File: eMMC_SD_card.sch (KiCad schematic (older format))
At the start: 0 parts

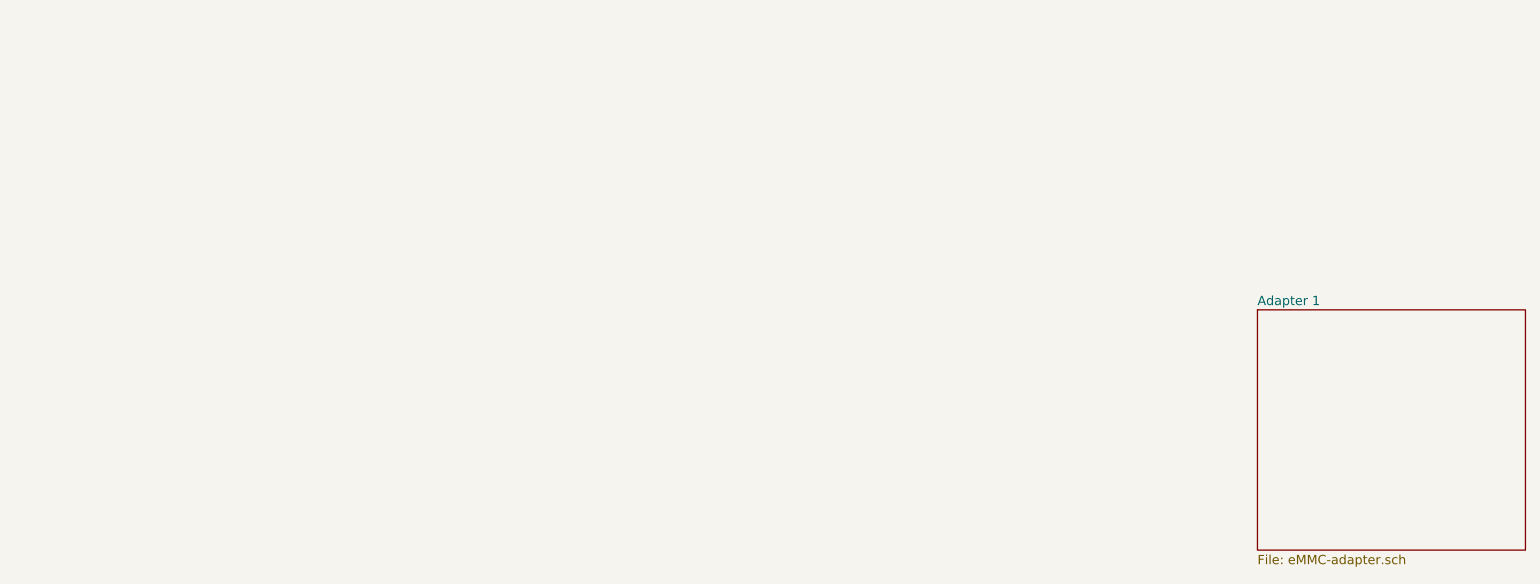
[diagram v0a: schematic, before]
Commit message: Panelize
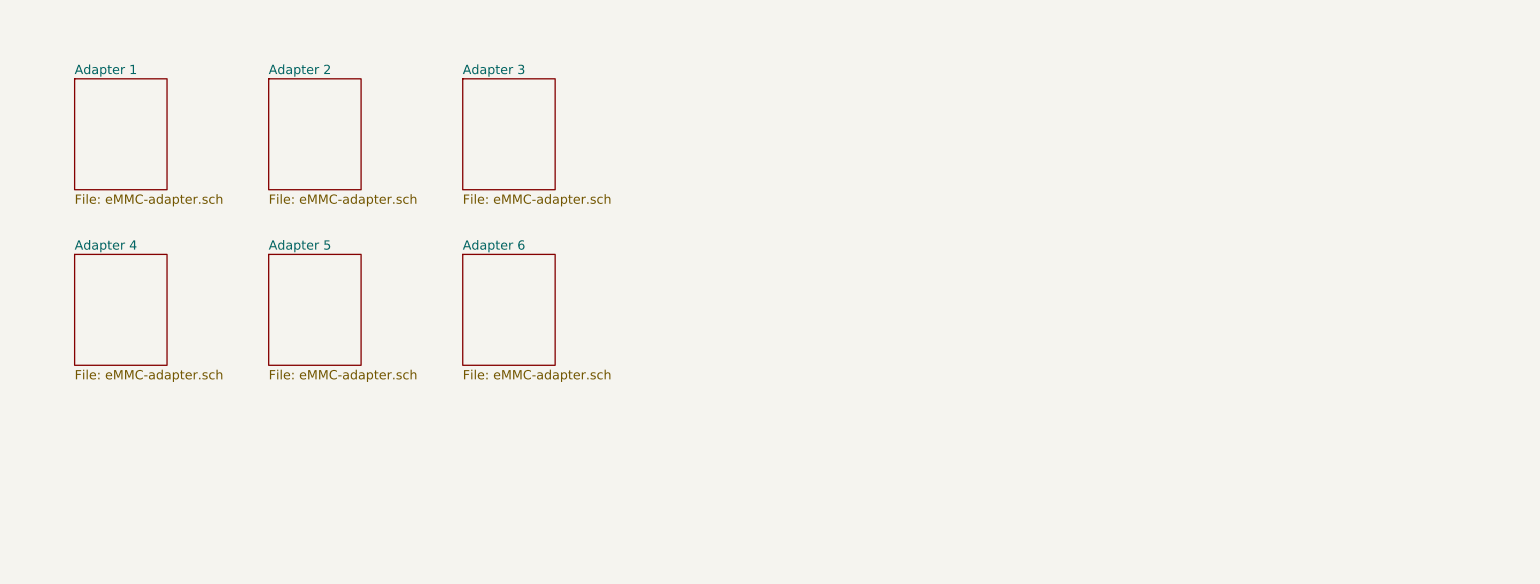
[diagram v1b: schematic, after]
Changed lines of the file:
@@
 $Descr A4 11693 8268
 encoding utf-8
-Sheet 1 2
+Sheet 1 7
 Title ""
 Date ""
@@
 $EndDescr
 $Sheet
-S 8350 2900 1450 1300
+S 1950 1650 500  600
 U 5FCA497B
 F0 "Adapter 1" 50
 F1 "eMMC-adapter.sch" 50
 $EndSheet
+$Sheet
+S 3000 1650 500  600
+U 5FD9515D
+F0 "Adapter 2" 50
+F1 "eMMC-adapter.sch" 50
+$EndSheet
+$Sheet
+S 4050 1650 500  600
+U 5FD951C9
+F0 "Adapter 3" 50
+F1 "eMMC-adapter.sch" 50
+$EndSheet
+$Sheet
+S 1950 2600 500  600
+U 5FD9521A
+F0 "Adapter 4" 50
+F1 "eMMC-adapter.sch" 50
+$EndSheet
+$Sheet
+S 3000 2600 500  600
+U 5FD9521C
+F0 "Adapter 5" 50
+F1 "eMMC-adapter.sch" 50
+$EndSheet
+$Sheet
+S 4050 2600 500  600
+U 5FD9521E
+F0 "Adapter 6" 50
+F1 "eMMC-adapter.sch" 50
+$EndSheet

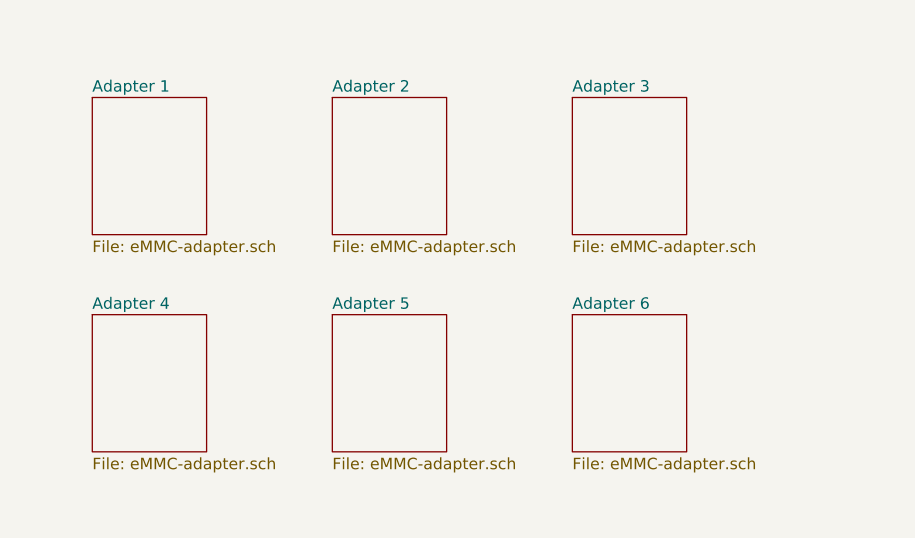
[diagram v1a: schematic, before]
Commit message: Add tooling holes
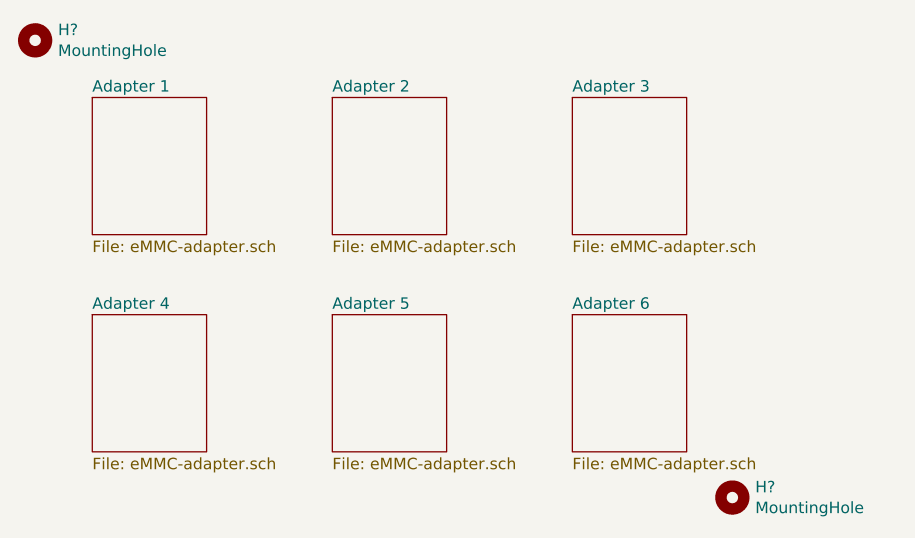
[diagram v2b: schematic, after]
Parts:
- added H? (x2): MountingHole, ToolingHole:ToolingHole_JLCSMT, symbol Mechanical:MountingHole
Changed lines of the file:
@@
 F1 "eMMC-adapter.sch" 50
 $EndSheet
+$Comp
+L Mechanical:MountingHole H?
+U 1 1 5FDC5AEE
+P 1700 1400
+F 0 "H?" H 1800 1446 50  0000 L CNN
+F 1 "MountingHole" H 1800 1355 50  0000 L CNN
+F 2 "ToolingHole:ToolingHole_JLCSMT" H 1700 1400 50  0001 C CNN
+F 3 "~" H 1700 1400 50  0001 C CNN
+	1    1700 1400
+	1    0    0    -1
+$EndComp
+$Comp
+L Mechanical:MountingHole H?
+U 1 1 5FDC62CD
+P 4750 3400
+F 0 "H?" H 4850 3446 50  0000 L CNN
+F 1 "MountingHole" H 4850 3355 50  0000 L CNN
+F 2 "ToolingHole:ToolingHole_JLCSMT" H 4750 3400 50  0001 C CNN
+F 3 "~" H 4750 3400 50  0001 C CNN
+	1    4750 3400
+	1    0    0    -1
+$EndComp
 $EndSCHEMATC

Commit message: Repurpose for ESP32 WiFi SDIO card
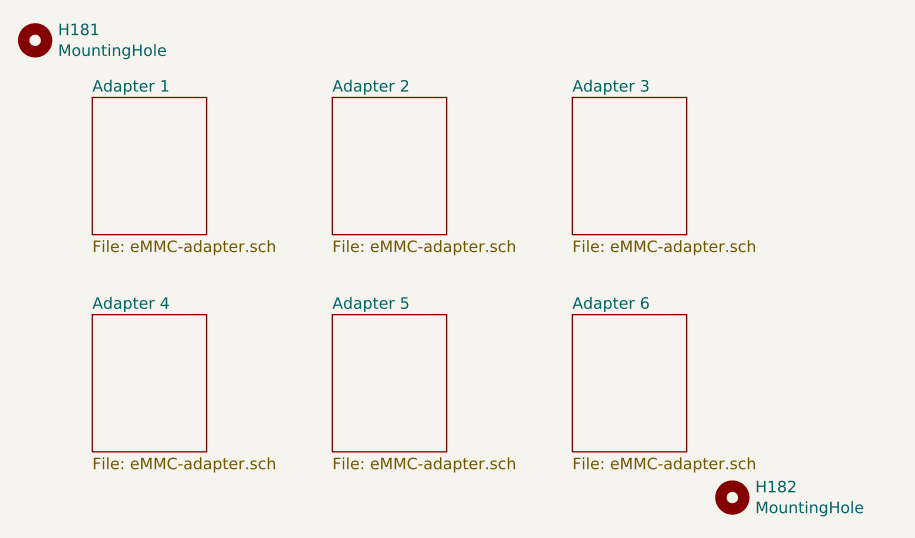
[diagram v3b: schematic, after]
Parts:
- gave numbers to parts that had none: 2
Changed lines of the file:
@@
 $EndSheet
 $Comp
-L Mechanical:MountingHole H?
+L Mechanical:MountingHole H181
 U 1 1 5FDC5AEE
 P 1700 1400
-F 0 "H?" H 1800 1446 50  0000 L CNN
+F 0 "H181" H 1800 1446 50  0000 L CNN
 F 1 "MountingHole" H 1800 1355 50  0000 L CNN
 F 2 "ToolingHole:ToolingHole_JLCSMT" H 1700 1400 50  0001 C CNN
@@
 $EndComp
 $Comp
-L Mechanical:MountingHole H?
+L Mechanical:MountingHole H182
 U 1 1 5FDC62CD
 P 4750 3400
-F 0 "H?" H 4850 3446 50  0000 L CNN
+F 0 "H182" H 4850 3446 50  0000 L CNN
 F 1 "MountingHole" H 4850 3355 50  0000 L CNN
 F 2 "ToolingHole:ToolingHole_JLCSMT" H 4750 3400 50  0001 C CNN
